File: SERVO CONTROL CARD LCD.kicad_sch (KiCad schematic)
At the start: 62 parts, among them J1 Conn_01x02, J2 Conn_01x02, J3 Conn_01x05, J4 Conn_01x02, J5 Conn_01x02, J6 Conn_01x03, K1 FINDER-34.51, Q1 BT136-500, Q2 BT136-500, Q3 BC547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

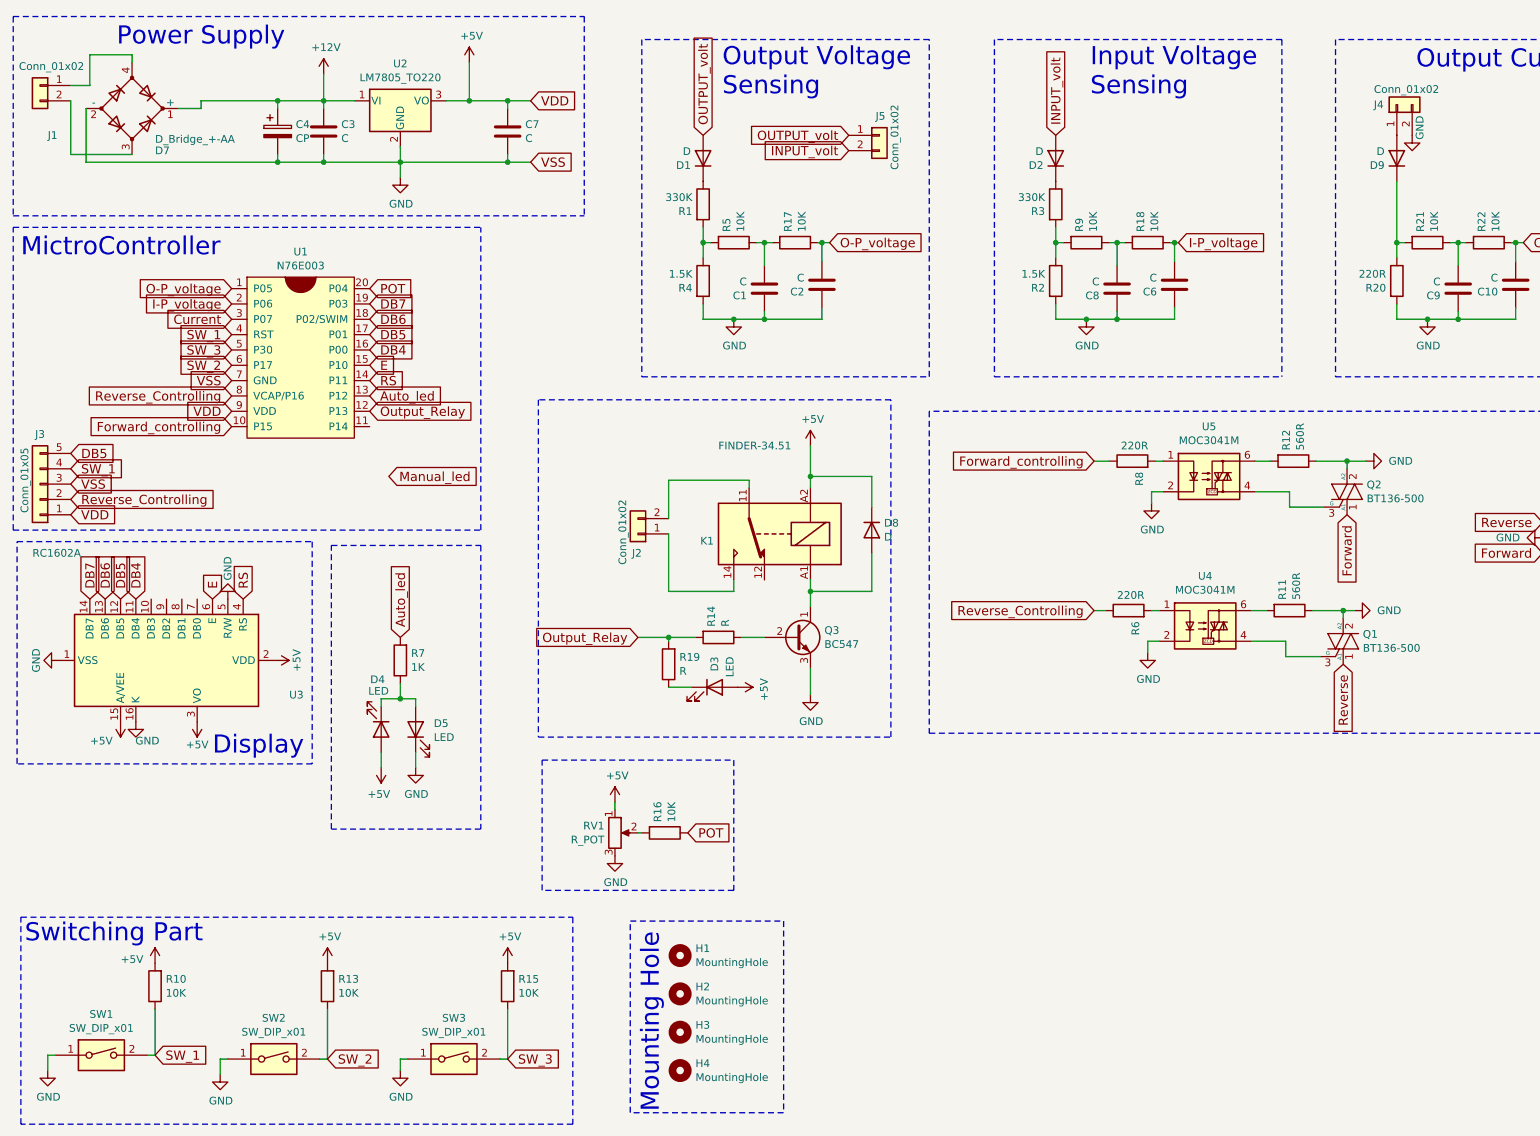
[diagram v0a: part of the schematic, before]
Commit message: pcb board hase standard size
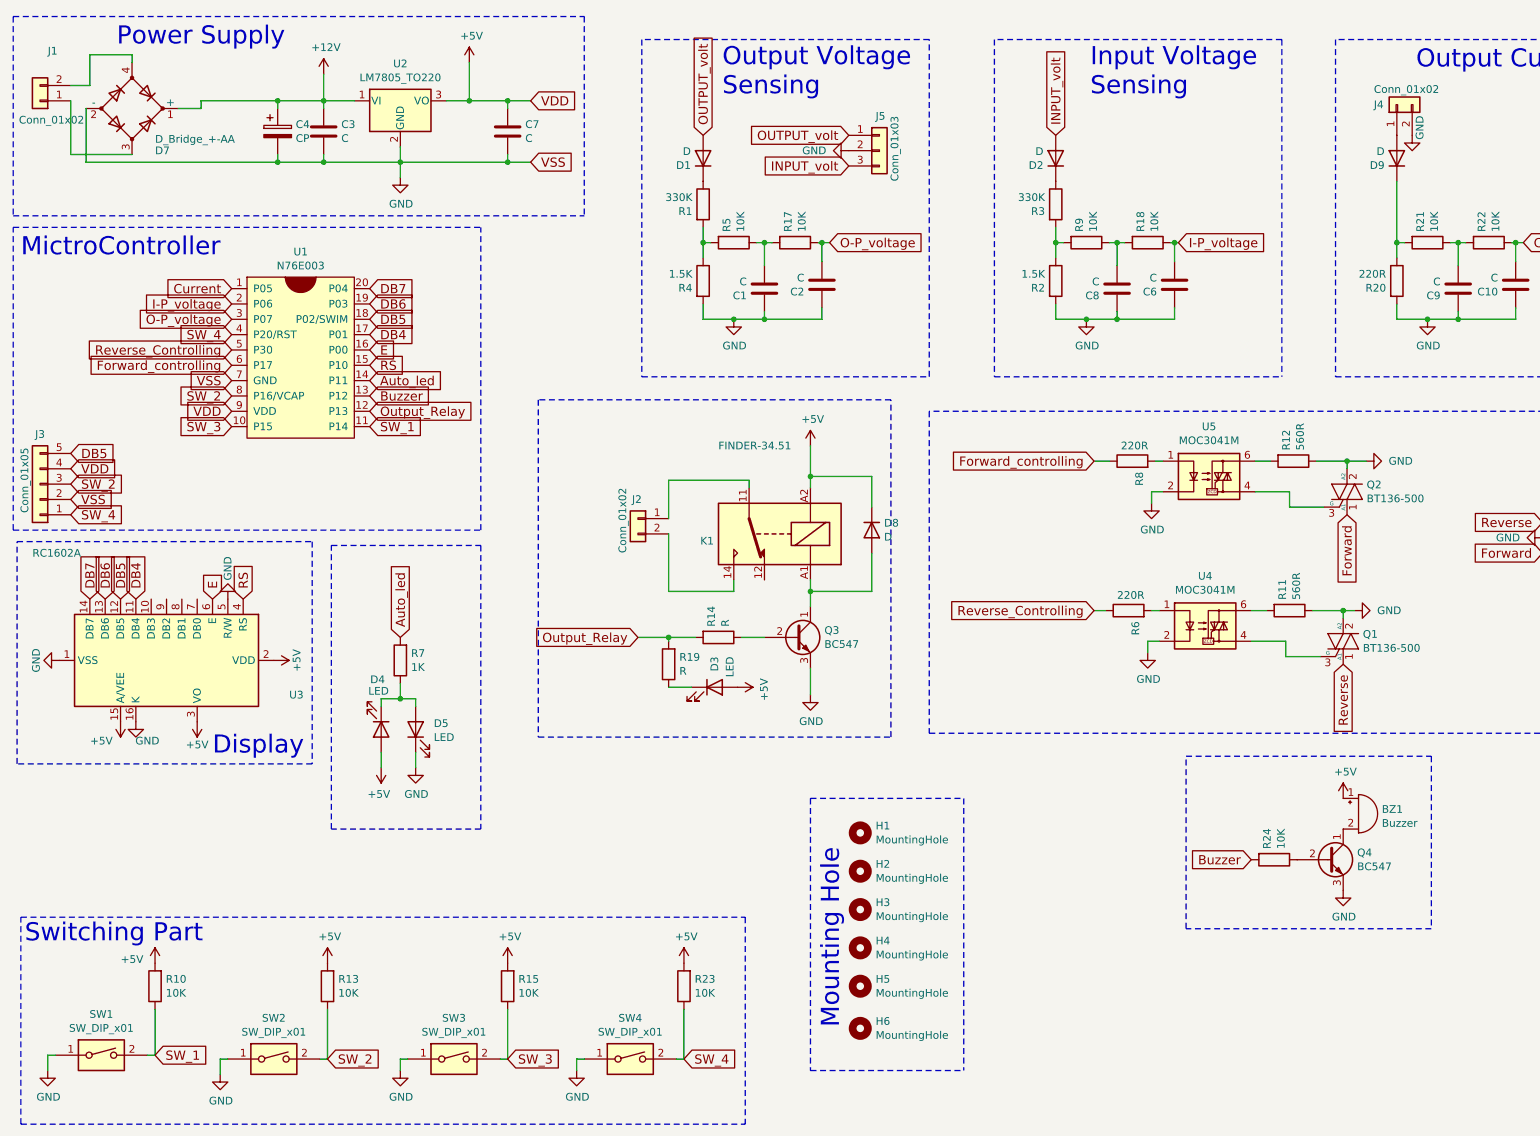
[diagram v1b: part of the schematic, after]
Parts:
- removed J5: Conn_01x02, Connector_JST:JST_NV_B02P-NV_1x02_P5.00mm_Vertical, symbol Connector_Generic:Conn_01x02
- removed R16: 10K, My Custom Footprint:R_1206_3216Metric, symbol Device:R
- removed RV1: R_POT, My Custom Footprint:Potentiometer_Trimmer_Bourns_3299Y, symbol Device:R_POT
- added BZ1: Buzzer, Buzzer_Beeper:Buzzer_12x9.5RM7.6, symbol Device:Buzzer
- added H5, H6: MountingHole, MountingHole:MountingHole_3.2mm_M3_Pad_Via, symbol Mechanical:MountingHole
- added J5: Conn_01x03, Connector_JST:JST_NV_B03P-NV_1x03_P5.00mm_Vertical, symbol Connector_Generic:Conn_01x03
- added Q4: BC547, My Custom Footprint:SOT-23_Transistor, symbol Transistor_BJT:BC547
- added R23, R24: 10K, My Custom Footprint:R_1206_3216Metric, symbol Device:R
- added SW4: SW_DIP_x01, Button_Switch_THT:SW_PUSH-12mm, symbol Switch:SW_DIP_x01
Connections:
- net POT is gone; now on net DB7: U1.20 (P04)
- net +5V: now also J3.4 (Pin_4), BZ1.1 (+), R23.2; no longer J3.1 (Pin_1)
- net Auto_led: now also U1.14 (P11); no longer U1.13 (P12)
- net Current: now also U1.1 (P05); no longer U1.3 (P07)
- net DB4: now also U1.17 (P01); no longer U1.16 (P00)
- net DB5: now also U1.18 (P02/SWIM); no longer U1.17 (P01)
- net DB6: now also U1.19 (P03); no longer U1.18 (P02/SWIM)
- net DB7: no longer U1.19 (P03)
- net E: now also U1.16 (P00); no longer U1.15 (P10)
- net Forward_controlling: now also U1.6 (P17); no longer U1.10 (P15)
- net GND: now also J3.2 (Pin_2), J5.2 (Pin_2), Q4.3 (E), SW4.1; no longer J3.3 (Pin_3)
- net INPUT_volt: now also J5.3 (Pin_3)
- net O-P_voltage: now also U1.3 (P07); no longer U1.1 (P05)
- net OUTPUT_volt: now also J5.1 (Pin_1)
- net RS: now also U1.15 (P10); no longer U1.14 (P11)
- net Reverse_Controlling: now also U1.5 (P30); no longer J3.2 (Pin_2), U1.8 (VCAP/P16)
- net SW_1: now also U1.11 (P14); no longer J3.4 (Pin_4), U1.4 (RST)
- net SW_2: now also J3.3 (Pin_3), U1.8 (P16/VCAP); no longer U1.6 (P17)
- net SW_3: now also U1.10 (P15); no longer U1.5 (P30)
- net at D7.3: now also J1.1 (Pin_1); no longer J1.2 (Pin_2)
- net at D7.4: now also J1.2 (Pin_2); no longer J1.1 (Pin_1)
- net at J2.1 (Pin_1): now also K1.11; no longer K1.14
- net at J2.2 (Pin_2): now also K1.14; no longer K1.11
- new net: BZ1.2 (-), Q4.1 (C)
- new net: Q4.2 (B), R24.1
- new net Buzzer: R24.2, U1.13 (P12)
- new net SW_4: J3.1 (Pin_1), R23.1, SW4.2, U1.4 (P20/RST)
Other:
- moved on the sheet: H1, H2, H3, H4, J1, J2

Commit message: pcb board hase standard size with block connector v1.2
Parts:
- removed J2: Conn_01x02, Connector_JST:JST_NV_B02P-NV_1x02_P5.00mm_Vertical, symbol Connector_Generic:Conn_01x02
- removed J4: Conn_01x02, Connector_JST:JST_EH_B2B-EH-A_1x02_P2.50mm_Vertical, symbol Connector_Generic:Conn_01x02
- removed J5, J6: Conn_01x03, Connector_JST:JST_NV_B03P-NV_1x03_P5.00mm_Vertical, symbol Connector_Generic:Conn_01x03
- added J2, J4: Conn_01x05, My Custom Footprint:Block_connector_5x1_H1.5_P8, symbol Connector_Generic:Conn_01x05
- J1: footprint Connector_JST:JST_EH_B2B-EH-A_1x02_P2.50mm_Vertical -> My Custom Footprint:Block_connector_2x1_H1.5_P8
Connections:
- net Forward: now also J4.1 (Pin_1)
- net GND: now also J2.1 (Pin_1), J2.4 (Pin_4), J4.2 (Pin_2)
- net INPUT_volt: now also J2.3 (Pin_3)
- net OUTPUT_volt: now also J2.5 (Pin_5)
- net Reverse: now also J4.3 (Pin_3)
- net at D7.3: now also J1.2 (Pin_2); no longer J1.1 (Pin_1)
- net at D7.4: now also J1.1 (Pin_1); no longer J1.2 (Pin_2)
- net Op_cutt1: now reaches K1.11
- net Op_cutt1: now also J4.5 (Pin_5)
- net Op_cutt2: now reaches K1.14
- net Op_cutt2: now also J4.4 (Pin_4)
- net CT_input: now reaches D9.2 (A)
- net CT_input: now also J2.2 (Pin_2)
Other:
- note added: "1. Update 1206 R & C"
- note added: "2. Update Block teminal 5x1 and 2x1"
- note added: "Note*"
- moved on the sheet: J1
